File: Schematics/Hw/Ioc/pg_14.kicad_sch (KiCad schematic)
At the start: 12 parts, among them U1501 F244, U1502 F244, U1503 F244, U1504 F244, U1505 F175, U1506 F74, U1507 F02, U1508 F74, U1509 F00, U1510 F00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

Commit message: Typos
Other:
- note added: "FFFFF800"
- note removed: "FFFFF000"
- note removed: "FFFFF001"
- note removed: "FFFFF002"
- note removed: "FFFFF003"
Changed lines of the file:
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@@
     (stroke (width 0) (type default))
   )
-  (text "FFFFF003\n" (at 81.28 363.22 0)
-    (effects (font (size 2.54 2.54)) (justify left bottom))
-  )
-  (text "FFFFF000\n" (at 81.28 106.68 0)
-    (effects (font (size 2.54 2.54)) (justify left bottom))
-  )
-  (text "FFFFF001\n\n" (at 81.28 198.12 0)
+  (text "FFFFF800\n" (at 81.28 106.68 0)
     (effects (font (size 2.54 2.54)) (justify left bottom))
   )
@@
     (effects (font (size 2.54 2.54)) (justify left bottom))
   )
-  (text "FFFFF002" (at 78.74 279.4 0)
-    (effects (font (size 2.54 2.54)) (justify left bottom))
-  )

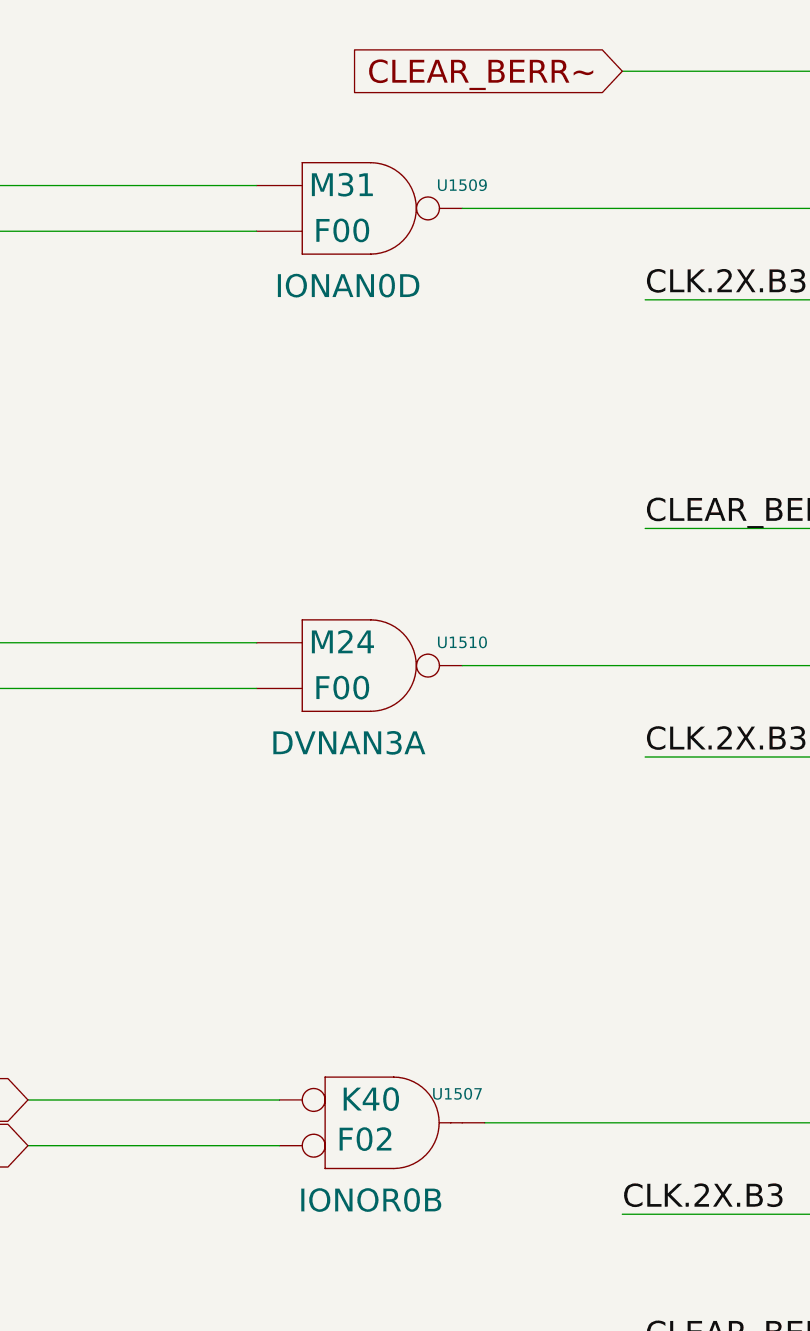
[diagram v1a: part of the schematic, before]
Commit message: Upgrade to KiCad9
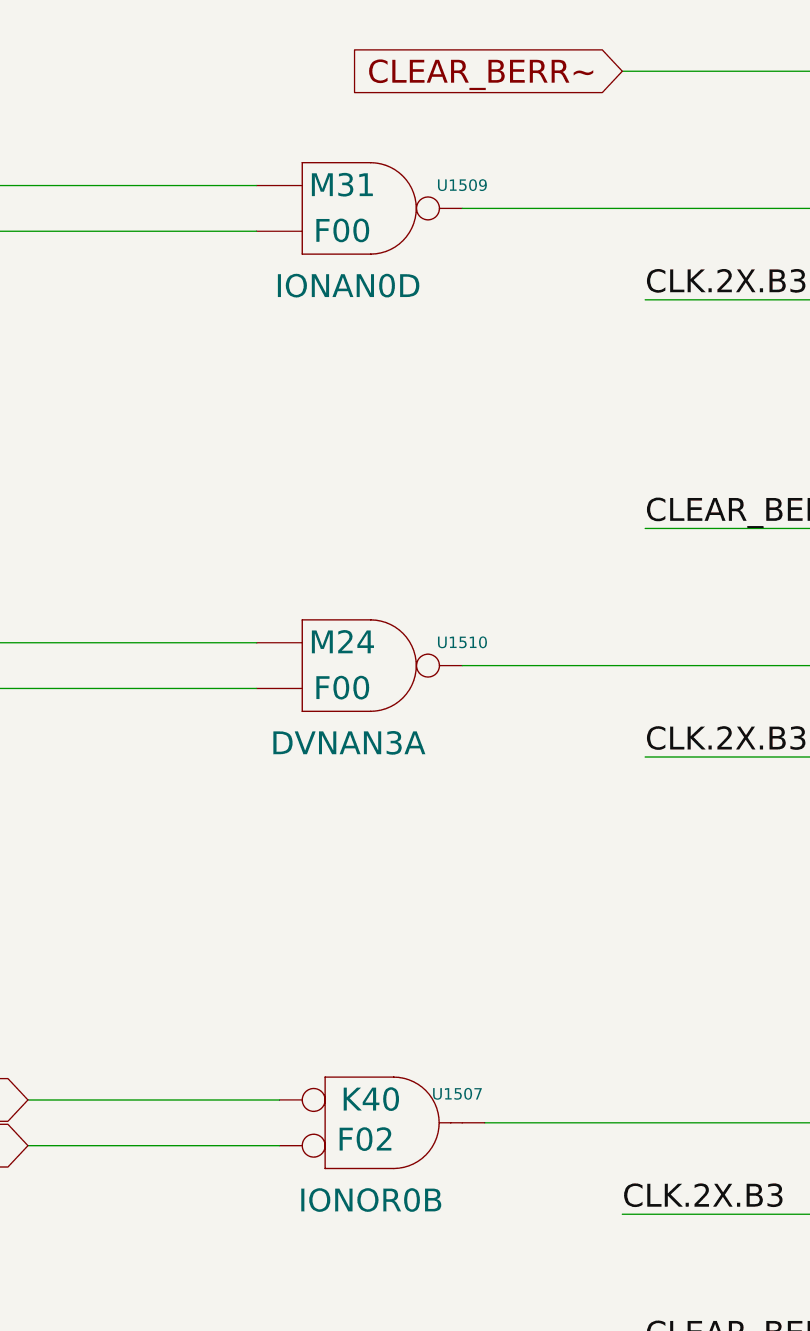
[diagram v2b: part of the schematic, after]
